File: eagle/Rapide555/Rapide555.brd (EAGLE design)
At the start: 50 x 34.8 mm, 23 parts, among them IC1 555, Q1 IRFZ44

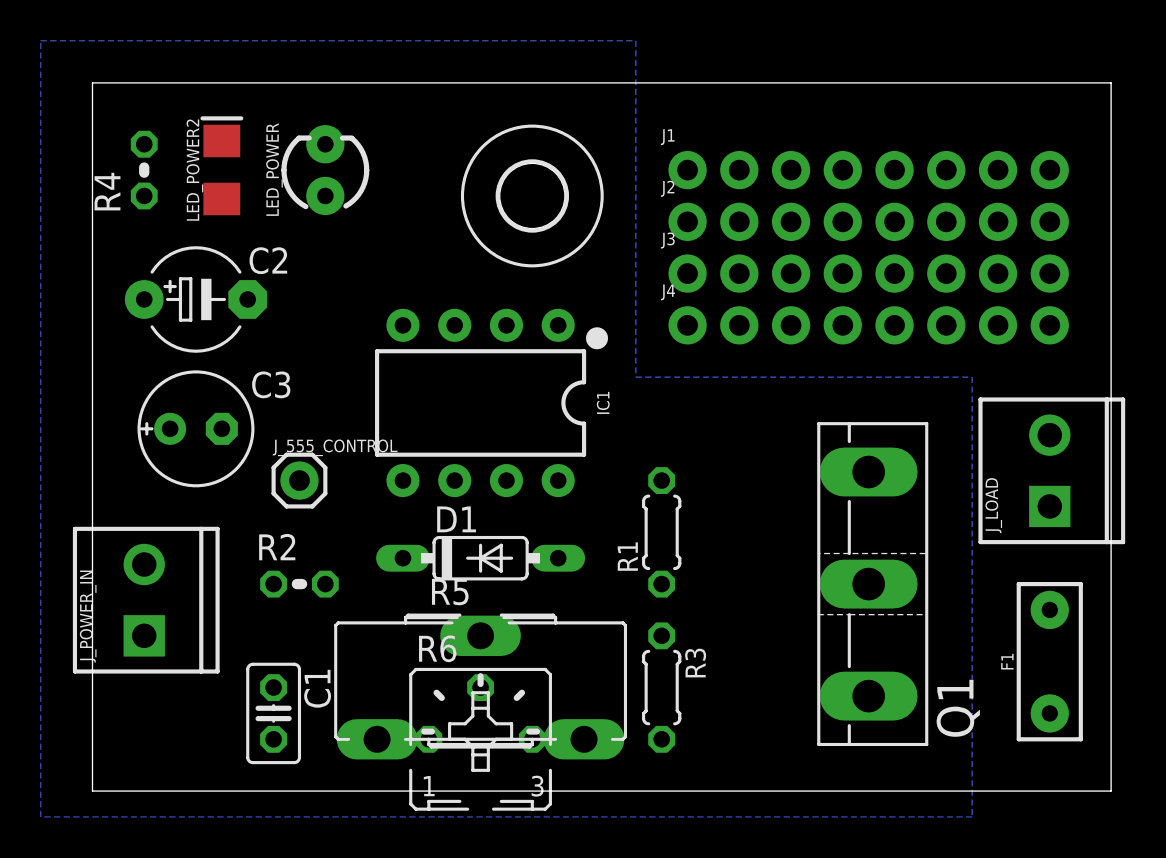
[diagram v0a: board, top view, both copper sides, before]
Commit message: Rapide555 board beta ok, need labels and review.
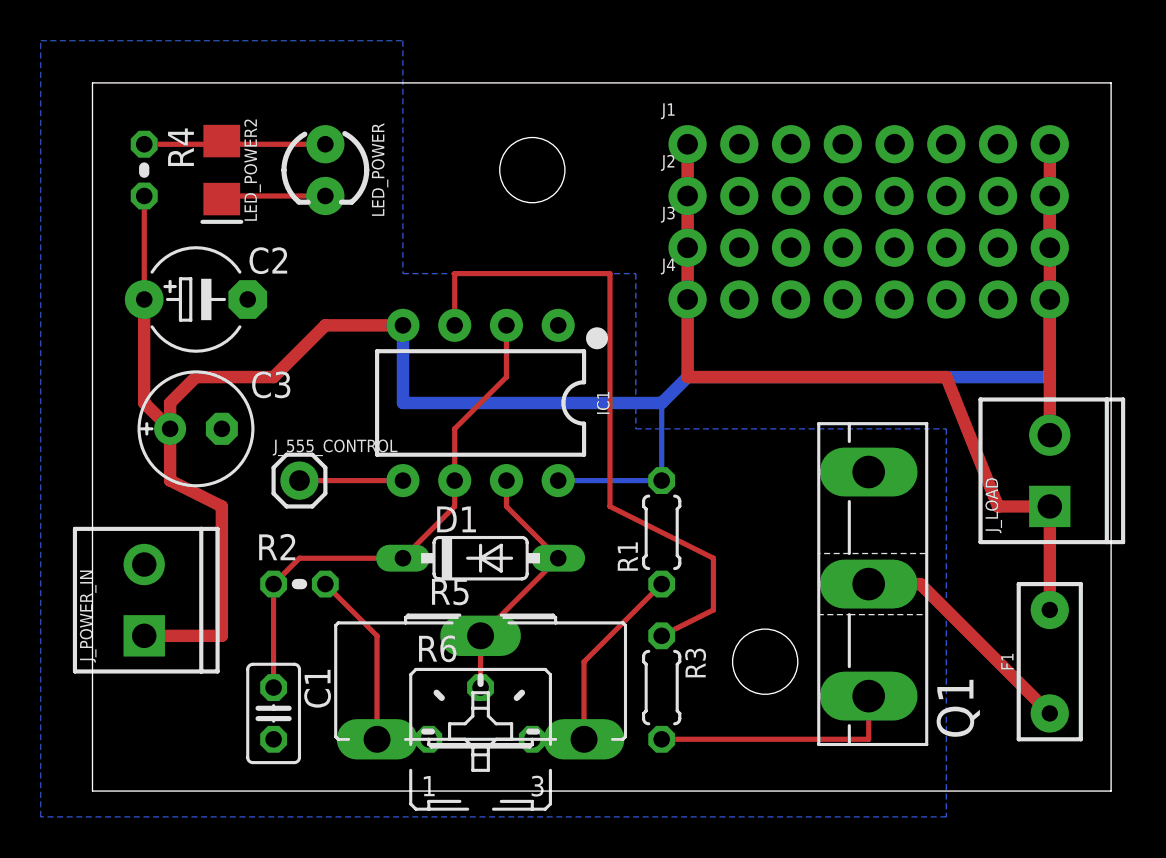
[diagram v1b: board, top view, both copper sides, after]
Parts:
- removed H1: MOUNT-HOLE3.2, holes:3,2
- moved J3 1.27 mm to (29.2, 26.7)
- moved J1 1.27 mm to (29.2, 31.8)
- moved J2 1.27 mm to (29.2, 29.2)
- moved J4 1.27 mm to (29.2, 24.1)
- turned LED_POWER to 270 degrees
- turned LED_POWER2 to 270 degrees
- turned R4 to 270 degrees
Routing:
- net VCC: track 0.00 -> 107.4 mm
- net N$2: track 0.00 -> 38.6 mm
- net N$5: track 0.00 -> 32.6 mm
- net N$7: track 0.00 -> 25.5 mm
- net N$1: track 0.00 -> 12.8 mm
- net N$6: track 0.00 -> 12.3 mm
- net N$8: track 0.00 -> 11.7 mm
- net N$3: track 0.00 -> 11.5 mm
- net N$9: track 0.00 -> 11.2 mm
- net N$12: track 0.00 -> 9.04 mm
- net GND: track 0.00 -> 5.23 mm
- net N$4: track 0.00 -> 5.08 mm

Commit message: Rapide555 minor changes.
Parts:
- moved R3 9.67 mm to (31.8, 14.0)
- moved R1 1.27 mm to (26.7, 12.7)
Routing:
- net N$5: track 32.6 -> 23.2 mm
- net N$6: track 12.3 -> 9.40 mm
- net N$2: track 38.6 -> 40.6 mm
- net VCC: track 107.4 -> 106.3 mm
- net N$8: track 11.7 -> 10.9 mm
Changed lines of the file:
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@@
 <wire x1="0" y1="34.76" x2="0" y2="0" width="0" layer="20"/>
 <hole x="21.59" y="30.48" drill="3.2"/>
-<hole x="33.02" y="6.35" drill="3.2"/>
+<hole x="30.48" y="5.08" drill="3.2"/>
 </plain>
 <attributes>
@@
 <attribute name="PROD_ID" value="RES-08490" x="87.63" y="30.48" size="1.778" layer="27" rot="R90" display="off"/>
 </element>
-<element name="R1" library="resistor" package="0204/5" value="100" x="27.94" y="12.7" rot="R90"/>
+<element name="R1" library="resistor" package="0204/5" value="100" x="26.67" y="12.7" rot="R90"/>
 <element name="R2" library="resistor" package="0204V" value="100" x="10.16" y="10.16"/>
-<element name="R3" library="resistor" package="0204/5" value="470" x="27.94" y="5.08" rot="R270"/>
+<element name="R3" library="resistor" package="0204/5" value="470" x="31.75" y="13.97" rot="R270"/>
 <element name="R4" library="resistor" package="0204V" value="1k" x="2.54" y="30.48" rot="R270"/>
 <element name="R5" library="pot" package="CA14H" value="" x="19.05" y="2.54"/>
@@
 <wire x1="3.81" y1="15.24" x2="6.35" y2="13.97" width="0.6096" layer="1"/>
 <wire x1="6.35" y1="13.97" x2="6.35" y2="7.62" width="0.6096" layer="1"/>
-<wire x1="22.86" y1="15.24" x2="27.94" y2="15.24" width="0.254" layer="16"/>
+<wire x1="22.86" y1="15.24" x2="26.67" y2="15.24" width="0.254" layer="16"/>
 <wire x1="46.99" y1="31.75" x2="46.99" y2="29.21" width="0.6096" layer="1"/>
 <wire x1="46.99" y1="26.67" x2="46.99" y2="24.13" width="0.6096" layer="1"/>
@@
 <wire x1="46.99" y1="26.67" x2="46.99" y2="29.21" width="0.6096" layer="16"/>
 <wire x1="29.21" y1="20.32" x2="27.94" y2="19.05" width="0.6096" layer="16"/>
-<wire x1="27.94" y1="19.05" x2="27.94" y2="15.24" width="0.254" layer="16"/>
+<wire x1="27.94" y1="19.05" x2="26.67" y2="15.24" width="0.254" layer="16"/>
 <wire x1="46.99" y1="20.32" x2="29.21" y2="20.32" width="0.6096" layer="16"/>
 <wire x1="46.99" y1="24.13" x2="46.99" y2="20.32" width="0.6096" layer="16"/>
@@
 <contactref element="IC1" pad="3"/>
 <contactref element="R3" pad="1"/>
-<wire x1="30.48" y1="8.89" x2="27.94" y2="7.62" width="0.254" layer="1"/>
-<wire x1="30.48" y1="11.43" x2="30.48" y2="8.89" width="0.254" layer="1"/>
-<wire x1="25.4" y1="13.97" x2="30.48" y2="11.43" width="0.254" layer="1"/>
-<wire x1="25.4" y1="25.4" x2="25.4" y2="13.97" width="0.254" layer="1"/>
+<wire x1="29.21" y1="16.51" x2="31.75" y2="16.51" width="0.254" layer="1"/>
+<wire x1="25.4" y1="20.32" x2="29.21" y2="16.51" width="0.254" layer="1"/>
+<wire x1="25.4" y1="25.4" x2="25.4" y2="20.32" width="0.254" layer="1"/>
 <wire x1="17.78" y1="25.4" x2="25.4" y2="25.4" width="0.254" layer="1"/>
 <wire x1="17.78" y1="22.86" x2="17.78" y2="25.4" width="0.254" layer="1"/>
@@
 <contactref element="R3" pad="2"/>
 <contactref element="Q1" pad="G"/>
-<wire x1="38.1" y1="2.54" x2="27.94" y2="2.54" width="0.254" layer="1"/>
-<wire x1="38.1" y1="4.66" x2="38.1" y2="2.54" width="0.254" layer="1"/>
+<wire x1="34.29" y1="7.62" x2="31.75" y2="11.43" width="0.254" layer="1"/>
+<wire x1="38.1" y1="4.66" x2="34.29" y2="7.62" width="0.254" layer="1"/>
 </signal>
 <signal name="N$7">
@@
 <contactref element="R6" pad="E"/>
 <wire x1="24.13" y1="2.54" x2="21.59" y2="2.54" width="0.254" layer="1"/>
-<wire x1="24.13" y1="6.35" x2="27.94" y2="10.16" width="0.254" layer="1"/>
+<wire x1="24.13" y1="6.35" x2="26.67" y2="10.16" width="0.254" layer="1"/>
 <wire x1="24.13" y1="2.54" x2="24.13" y2="6.35" width="0.254" layer="1"/>
 </signal>
@@
 <wire x1="29.21" y1="31.75" x2="29.21" y2="29.21" width="0.6096" layer="1"/>
 <wire x1="29.21" y1="29.21" x2="29.21" y2="26.67" width="0.6096" layer="1"/>
-<wire x1="29.21" y1="20.32" x2="41.91" y2="20.32" width="0.6096" layer="1"/>
-<wire x1="41.91" y1="20.32" x2="44.45" y2="13.97" width="0.6096" layer="1"/>
-<wire x1="44.45" y1="13.97" x2="46.99" y2="13.97" width="0.6096" layer="1"/>
+<wire x1="29.21" y1="20.32" x2="43.18" y2="20.32" width="0.6096" layer="1"/>
+<wire x1="43.18" y1="20.32" x2="43.18" y2="13.97" width="0.6096" layer="1"/>
+<wire x1="43.18" y1="13.97" x2="46.99" y2="13.97" width="0.6096" layer="1"/>
 <wire x1="29.21" y1="24.13" x2="29.21" y2="20.32" width="0.6096" layer="1"/>
 </signal>

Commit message: Added labels, ready for production
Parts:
- removed R5: (no value), pot:CA14H
- moved R6 1.80 mm to (20.3, 3.81)
- moved R2 1.80 mm to (11.4, 8.89)
- moved J_POWER_IN 1.27 mm to (3.81, 7.62)
- moved C1 1.27 mm to (10.2, 3.81)
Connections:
- net N$1: no longer R5.S
- net N$8: no longer R5.E
- net N$9: no longer R5.A
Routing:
- net N$3: track 11.5 -> 15.2 mm
- net VCC: track 106.3 -> 105.0 mm
- net N$9: track 11.2 -> 10.2 mm
- net N$8: track 10.9 -> 10.2 mm
- net N$7: track 25.5 -> 25.0 mm
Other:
- board text added: "GND"
- board text added: "PWM"
- board text added: "PWM555"
- board text added: "VCC"
- board text added: "http://electrogeek.cc/rapide555.html"
